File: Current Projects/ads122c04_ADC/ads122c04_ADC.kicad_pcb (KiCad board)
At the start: 2 copper layers, 50.8 x 25.4 mm, 32 parts, among them J1 Conn_01x05, J2 Conn_01x04, U1 ADS122C04IPWR, U2 MCP1755ST-3302E/DB

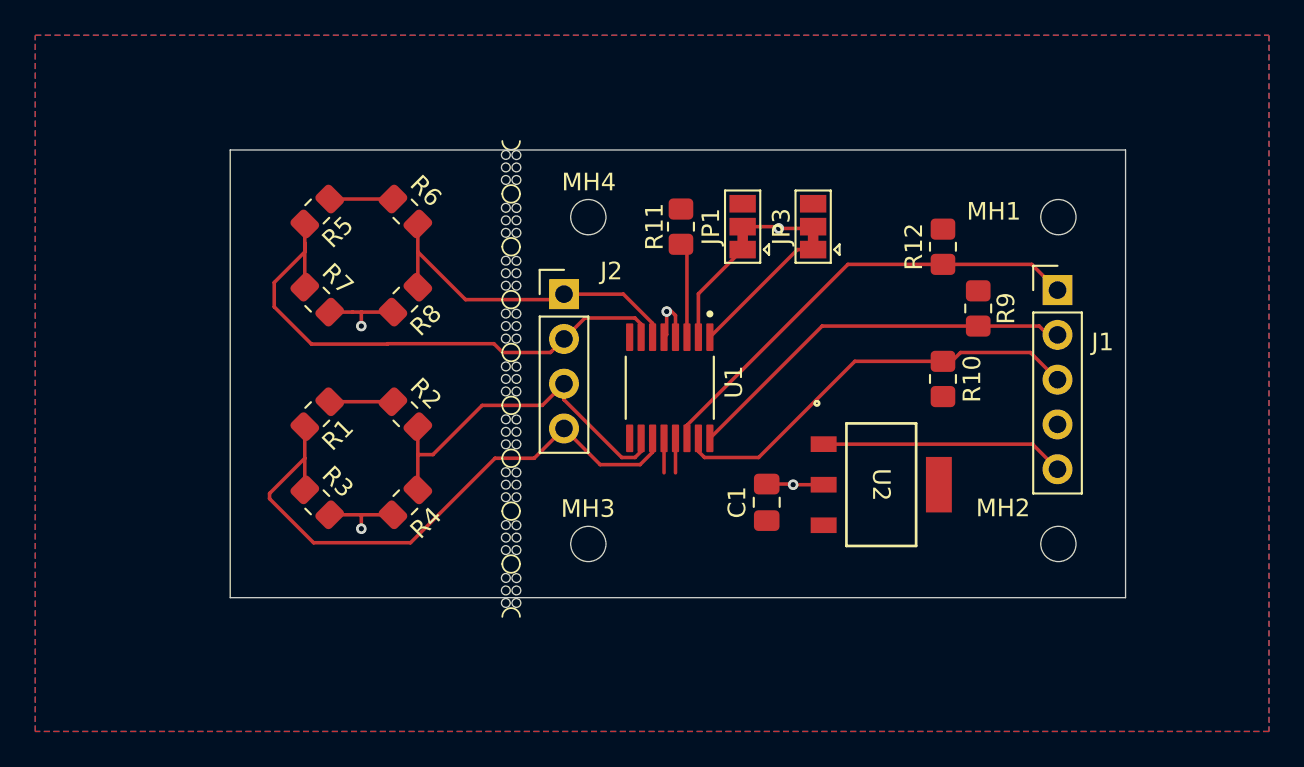
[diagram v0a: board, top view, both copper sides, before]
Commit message: ADC board with changes from Jacobs review.
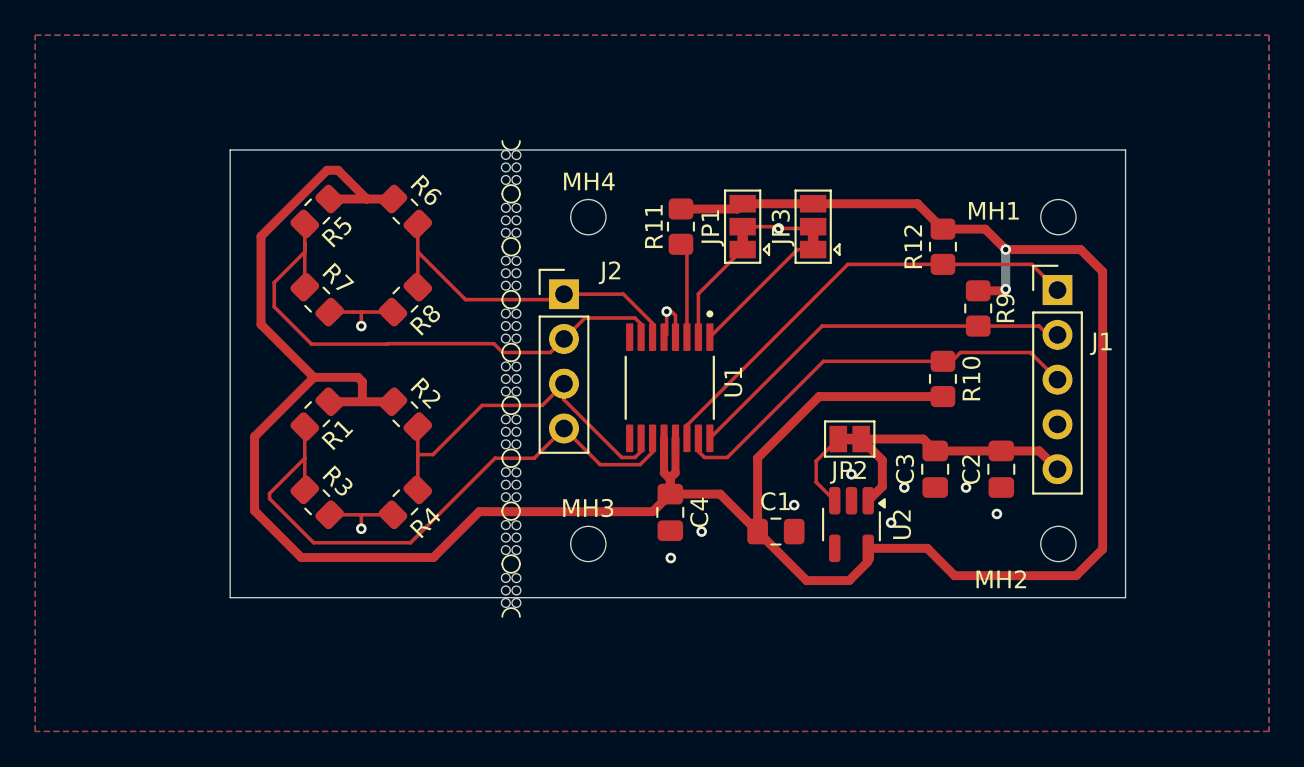
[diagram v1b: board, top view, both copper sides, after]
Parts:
- added C2: 2.2u, Capacitor_SMD:C_0805_2012Metric_Pad1.18x1.45mm_HandSolder, F.Cu at (142.8, 98.1)
- added C3: 10u, Capacitor_SMD:C_0805_2012Metric_Pad1.18x1.45mm_HandSolder, F.Cu at (139.1, 98.1)
- added C4: 0.1u, Capacitor_SMD:C_0805_2012Metric_Pad1.18x1.45mm_HandSolder, F.Cu at (124.0, 100.6)
- added JP2: SolderJumper_2_Bridged, Jumper:SolderJumper-2_P1.3mm_Bridged_Pad1.0x1.5mm, F.Cu at (134.2, 96.4)
- U2: value MCP1755ST-3302E/DB -> MCP1711T-33I/OT; footprint Custom_Lin_Reg:SOT-223_3MC_MCH -> Package_TO_SOT_SMD:SOT-23-5_HandSoldering
- moved U2 2.82 mm to (134.3, 101.3)
- moved C1 1.74 mm to (130.0, 101.7), turned to 0 degrees
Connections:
- U2 pad 3: +3.3V -> Net-(JP2-B)
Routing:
- net +3.3V: track 11.6 -> 160.5 mm, vias 0 -> 2
- net Net-(JP2-B): track 0.00 -> 4.45 mm
- net GND: track 19.5 -> 16.8 mm, vias 5 -> 12
- net +5V: track 13.9 -> 16.2 mm
- added copper zone on F.Cu, net GND
- removed copper zone on F.Cu, net +3.3V

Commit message: Increased trace widths, added silkscreen doodle, adding proper filtering caps for power signals, increased board size to 2x1.1, and swapped voltage regulator with proper one.
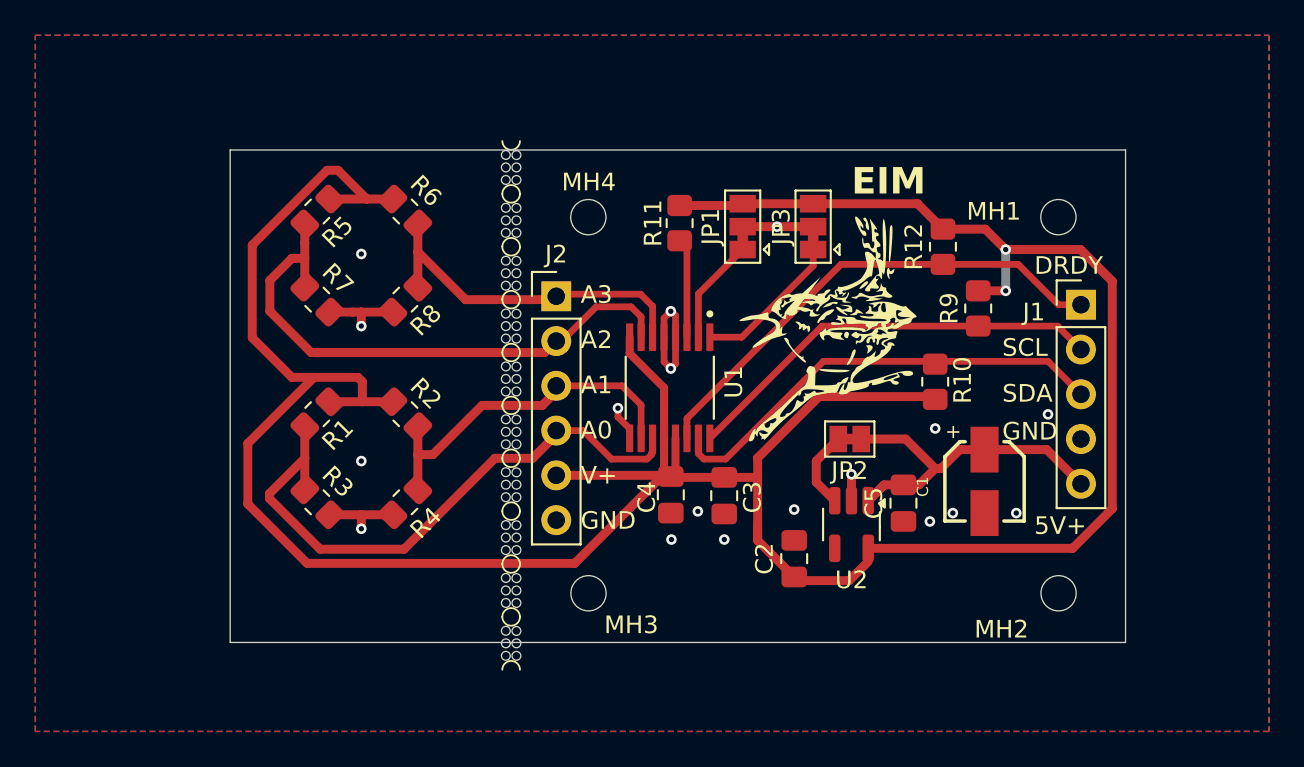
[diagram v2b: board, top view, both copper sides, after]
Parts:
- removed the C2 at (142.8, 98.1)
- added C1: 10u, 865080340001:WCAP-ASLI_4X5.5_DXL_, F.Cu at (141.9, 98.8)
- added C5: 1u, Capacitor_SMD:C_0805_2012Metric_Pad1.18x1.45mm_HandSolder, F.Cu at (137.3, 100.0)
- added mouse-bite-1mm-3mm: VAL**, mouse-bite.pretty-main:mouse-bite-1mm-3mm, F.Cu at (115.0, 108.0)
- C2: renamed from C1; value 2.2u -> 1u
- C3: value 10u -> 1u
- J2: value Conn_01x04 -> Conn_01x06; footprint Connector_PinHeader_2.54mm:PinHeader_1x04_P2.54mm_Vertical -> Connector_PinHeader_2.54mm:PinHeader_1x06_P2.54mm_Vertical
- moved C3 12.1 mm to (127.1, 99.6), turned to -90 degrees
- moved MH2 2.80 mm to (146.1, 105.2)
- moved MH3 2.80 mm to (119.4, 105.2)
- moved C2 1.85 mm to (131.1, 103.2), turned to 90 degrees
- moved J1 1.57 mm to (147.3, 88.8)
- moved C4 1.00 mm to (124.1, 99.6)
- moved R10 0.47 mm to (139.1, 93.2)
- moved J2 0.46 mm to (117.6, 88.3)
- moved R11 0.21 mm to (124.6, 84.2)
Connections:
- C3 pad 1: GND -> +3.3V
- C3 pad 2: +5V -> GND
- U1 pad 8: unconnected-(U1-REFN-Pad8) -> +3.3V
- U1 pad 9: unconnected-(U1-REFP-Pad9) -> GND
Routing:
- net +3.3V: track 160.5 -> 172.3 mm
- net GND: track 16.8 -> 23.8 mm, vias 12 -> 18
- net +5V: track 16.2 -> 20.1 mm
- net /DRDY: track 26.2 -> 28.1 mm
- net /SCL: track 22.6 -> 24.2 mm
- net /SDA: track 24.4 -> 25.8 mm
- net /G1+: track 31.5 -> 32.3 mm
- net /G0-: track 21.1 -> 20.3 mm
- net /G1-: track 19.6 -> 20.2 mm
- net /A0: track 7.92 -> 8.46 mm
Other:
- board size 50.8 x 25.4 mm -> 50.8 x 27.9 mm
- board text added: "5V+"
- board text added: "A0"
- board text added: "A1"
- board text added: "A2"
- board text added: "A3"
- board text added: "DRDY"
- board text added: "EIM"
- board text added: "GND"
- board text added: "SCL"
- board text added: "SDA"
- board text added: "V+"

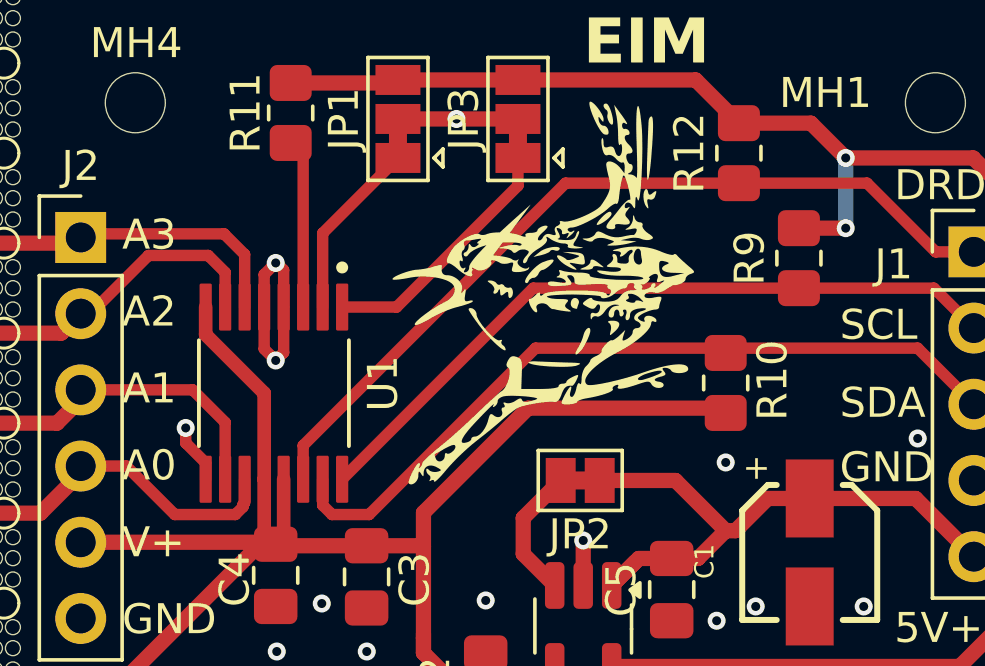
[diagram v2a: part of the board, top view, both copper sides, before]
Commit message: Made ADC traces straight out from ADC
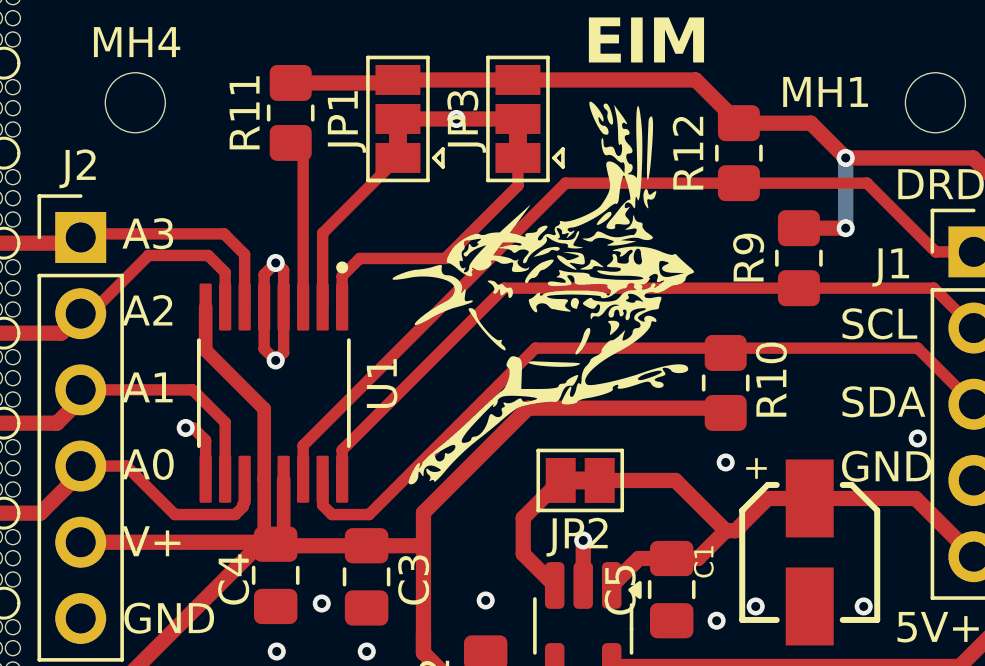
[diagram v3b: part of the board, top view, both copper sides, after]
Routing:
- net /A0: track 8.46 -> 9.07 mm
- net /SCL: track 24.2 -> 24.8 mm
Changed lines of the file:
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@@
-	)
-	(segment
-		(start 123.675 96.37)
-		(end 123.675 93.498946)
-		(width 0.4572)
-		(layer "F.Cu")
-		(net 1)
 	)
 	(segment
@@
 	)
 	(segment
-		(start 121.725001 91.548947)
-		(end 121.725001 90.63)
+		(start 123.675 96.37)
+		(end 123.675 94.025)
 		(width 0.4572)
 		(layer "F.Cu")
@@
 		(end 105.177107 81.16)
 		(width 0.508)
-		(layer "F.Cu")
-		(net 1)
-	)
-	(segment
-		(start 123.675 93.498946)
-		(end 121.725001 91.548947)
-		(width 0.4572)
 		(layer "F.Cu")
 		(net 1)
@@
 	)
 	(segment
+		(start 121.725001 92.075001)
+		(end 121.725001 90.63)
+		(width 0.4572)
+		(layer "F.Cu")
+		(net 1)
+	)
+	(segment
 		(start 128.135 83.06)
 		(end 132.135 83.06)
@@
 	)
 	(segment
+		(start 123.675 94.025)
+		(end 121.725001 92.075001)
+		(width 0.4572)
+		(layer "F.Cu")
+		(net 1)
+	)
+	(segment
 		(start 124.56 83.16)
 		(end 128.035 83.16)
@@
 	)
 	(segment
-		(start 121.725001 95.825001)
-		(end 121.725001 96.37)
-		(width 0.381)
-		(layer "F.Cu")
-		(net 2)
-	)
-	(segment
 		(start 124.088374 89.16)
 		(end 124.325 89.396626)
@@
 	)
 	(segment
-		(start 121.06 94.66)
-		(end 121.06 95.16)
+		(start 121.725001 95.075001)
+		(end 121.725001 96.37)
 		(width 0.381)
 		(layer "F.Cu")
@@
 	)
 	(segment
+		(start 121.06 94.66)
+		(end 121.31 94.66)
+		(width 0.381)
+		(layer "F.Cu")
+		(net 2)
+	)
+	(segment
 		(start 124.325 92.145)
 		(end 124.06 92.41)
@@
 	)
 	(segment
+		(start 121.31 94.66)
+		(end 121.725001 95.075001)
+		(width 0.381)
+		(layer "F.Cu")
+		(net 2)
+	)
+	(segment
 		(start 108.292893 89.207107)
 		(end 106.5 89.207107)
@@
 	)
 	(segment
-		(start 121.06 95.16)
-		(end 121.725001 95.825001)
-		(width 0.381)
-		(layer "F.Cu")
-		(net 2)
-	)
-	(segment
 		(start 106.5 89.207107)
 		(end 106 89.207107)
@@
 	)
 	(segment
+		(start 131.67 90)
+		(end 141.5 90)
+		(width 0.381)
+		(layer "F.Cu")
+		(net 3)
+	)
+	(segment
 		(start 141.5 90)
 		(end 146 90)
@@
 	)
 	(segment
+		(start 126.274999 96.37)
+		(end 126.274999 95.395001)
+		(width 0.381)
+		(layer "F.Cu")
+		(net 3)
+	)
+	(segment
 		(start 146 90)
 		(end 147.33 91.33)
@@
 	)
 	(segment
-		(start 132.644999 90)
-		(end 141.5 90)
-		(width 0.381)
-		(layer "F.Cu")
-		(net 3)
-	)
-	(segment
-		(start 126.274999 96.37)
-		(end 132.644999 90)
+		(start 126.274999 95.395001)
+		(end 131.67 90)
 		(width 0.381)
 		(layer "F.Cu")
@@
 	)
 	(segment
-		(start 128.09 90.63)
+		(start 126.274999 89.595001)
 		(end 126.274999 90.63)
 		(width 0.381)
@@
 	(segment
 		(start 132.135 86.585)
-		(end 128.09 90.63)
-		(width 0.381)
-		(layer "F.Cu")
+		(end 129.71 89.01)
+		(width 0.381)
+		(layer "F.Cu")
+		(net 12)
+	)
+	(segment
+		(start 129.71 89.01)
+		(end 126.86 89.01)
+		(width 0.381)
+		(layer "F.Cu")
+		(net 12)
+	)
+	(segment
+		(start 126.86 89.01)
+		(end 126.274999 89.595001)
+		(width 0.381)
+		(layer "F.Cu")
